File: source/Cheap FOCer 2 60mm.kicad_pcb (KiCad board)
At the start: 2 copper layers, 59.1 x 99.9 mm, 216 parts, among them J1 Conn_01x02, J2 Conn_01x07, J3 Conn_01x03, J4 On/Off, J5 UNUSED MCU PINS, J6 Conn_01x03, P1 MOTOR1, P2 MOTOR1, P3 MOTOR1, P4 HALL/Encoder, P5 SWD, Q1 NCEP60T20, Q2 NCEP60T20, Q3 NCEP60T20, Q4 NCEP60T20, Q5 NCEP60T20, Q6 NCEP60T20, U1 AMS1117-3.3, U2 DRV8301, U3 TP2604-SR, U4 TJA1051T/3/1J, U5 STM32F405RGT6, U6 BMI160, X1 8MHz 10ppm (X50328MSB2GI)

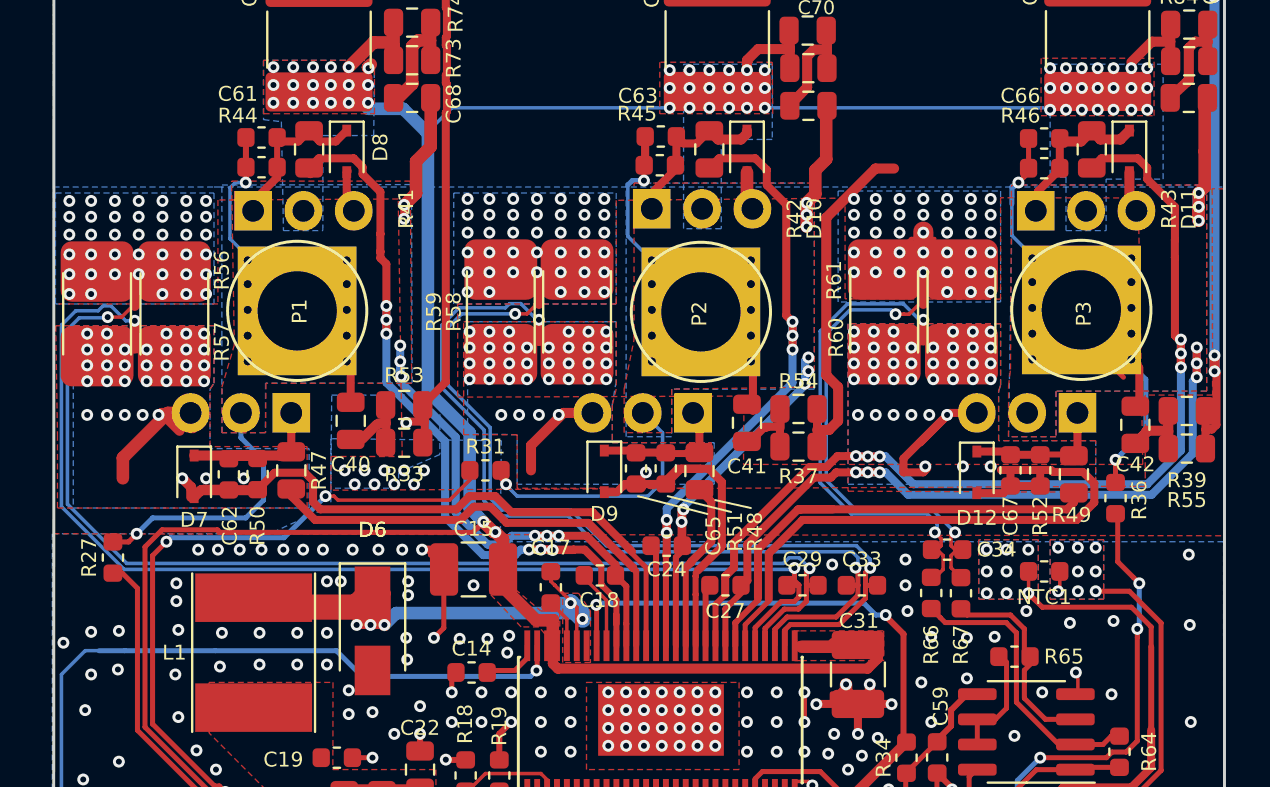
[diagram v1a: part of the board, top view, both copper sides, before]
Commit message: Revert "Remove transistors"
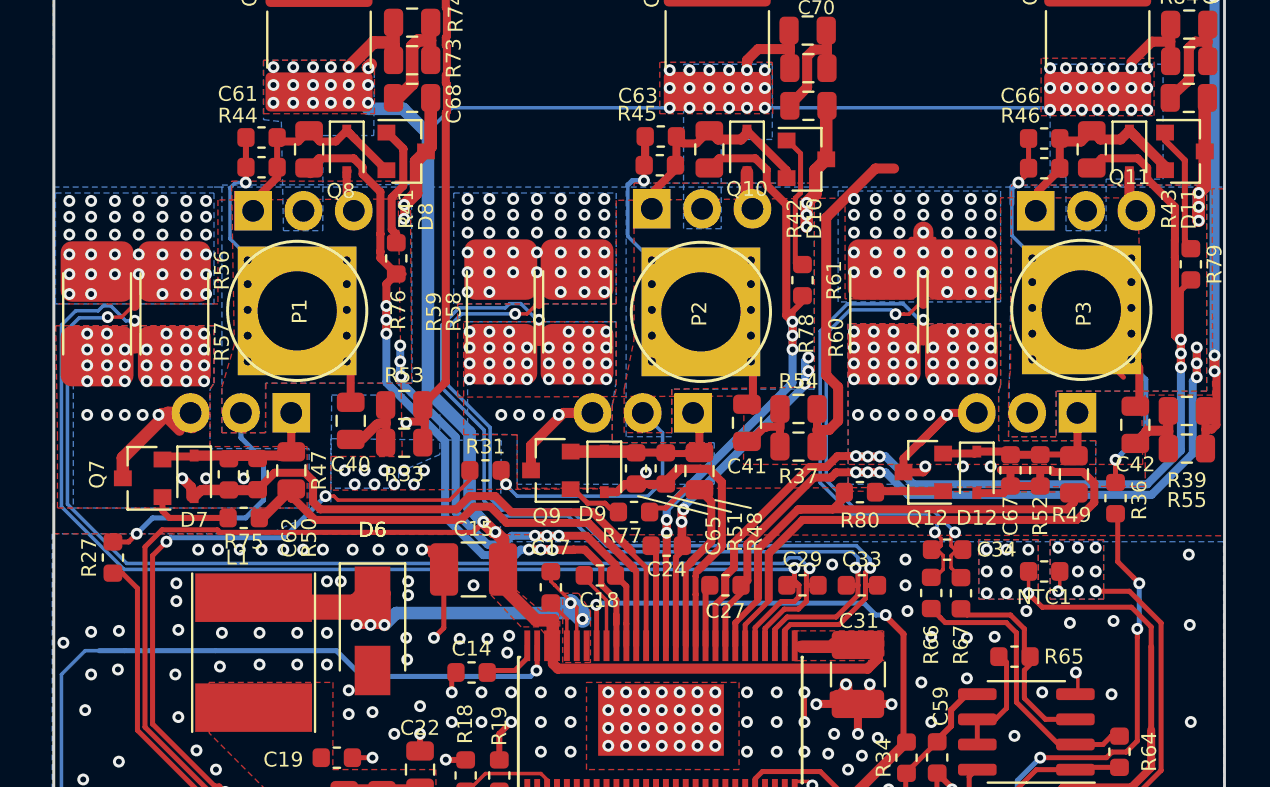
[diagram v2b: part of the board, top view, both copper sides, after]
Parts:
- added Q10: Q_PNP_BCE, Package_TO_SOT_SMD:SOT-23, F.Cu at (148.6, 93.8)
- added Q11: Q_PNP_BCE, Package_TO_SOT_SMD:SOT-23, F.Cu at (167.7, 93.4)
- added Q12: Q_PNP_BCE, Package_TO_SOT_SMD:SOT-23, F.Cu at (154.5, 109.6)
- added Q7: Q_PNP_BCE, Package_TO_SOT_SMD:SOT-23, F.Cu at (115.1, 109.9)
- added Q8: Q_PNP_BCE, Package_TO_SOT_SMD:SOT-23, F.Cu at (128.4, 93.4)
- added Q9: Q_PNP_BCE, Package_TO_SOT_SMD:SOT-23, F.Cu at (135.7, 109.5)
- added R75: 4.7R, Resistor_SMD:R_0603_1608Metric, F.Cu at (120.2, 111.9)
- added R76: 4.7R, Resistor_SMD:R_0603_1608Metric, F.Cu at (127.9, 98.8)
- added R77: 4.7R, Resistor_SMD:R_0603_1608Metric, F.Cu at (139.9, 111.6)
- added R78: 4.7R, Resistor_SMD:R_0603_1608Metric, F.Cu at (148.4, 99.9)
- added R79: 4.7R, Resistor_SMD:R_0603_1608Metric, F.Cu at (168.0, 99.1)
- added R80: 4.7R, Resistor_SMD:R_0603_1608Metric, F.Cu at (151.3, 110.6)
- R41, R42, R43, R47, R48, R49: value 10R -> 4.7R
- R56, R57, R58, R59, R60, R61: value 0.001R -> 0.002R
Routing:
- net Net-(Q10-Pad1): track 0.00 -> 7.33 mm
- net Net-(Q11-Pad1): track 0.00 -> 6.73 mm
- net Net-(Q8-Pad1): track 0.00 -> 6.63 mm
- net Net-(Q7-Pad1): track 0.00 -> 4.16 mm
- net Net-(C61-Pad1): track 10.4 -> 14.1 mm
- net /Mosfet driver/GH_C: track 54.3 -> 58.0 mm
- net Net-(Q12-Pad1): track 0.00 -> 3.60 mm
- net Net-(C66-Pad1): track 9.52 -> 12.8 mm
- net Net-(C65-Pad1): track 9.83 -> 13.1 mm
- net Net-(C63-Pad1): track 10.1 -> 13.3 mm
- net /Mosfet driver/GL_B: track 9.06 -> 12.0 mm
- net Net-(Q9-Pad1): track 0.00 -> 2.81 mm
- net Net-(C62-Pad1): track 12.0 -> 14.6 mm
- net /Mosfet driver/GL_A: track 23.7 -> 26.0 mm
- net Net-(C67-Pad1): track 7.23 -> 8.97 mm
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
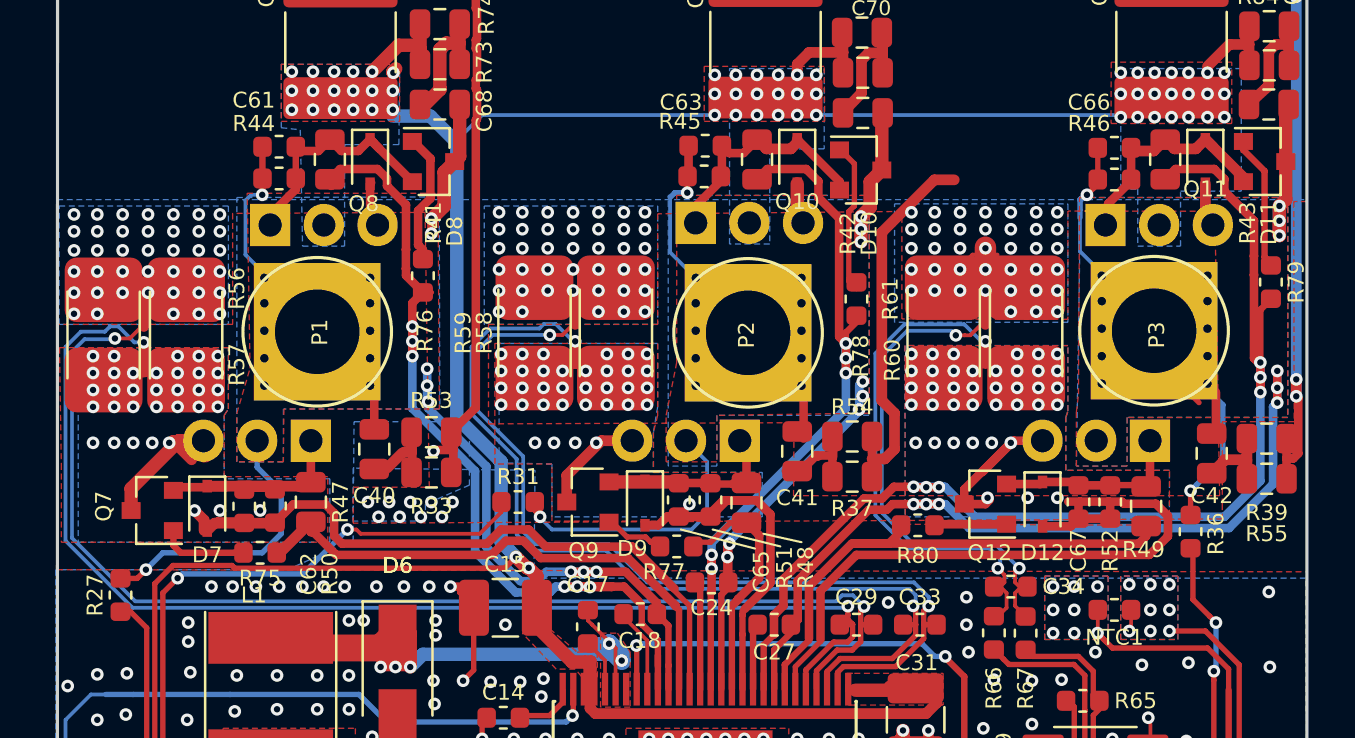
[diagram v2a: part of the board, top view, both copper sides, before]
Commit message: removed transistors from the gate of the mosfets and fixed the config file for compiling the firmware
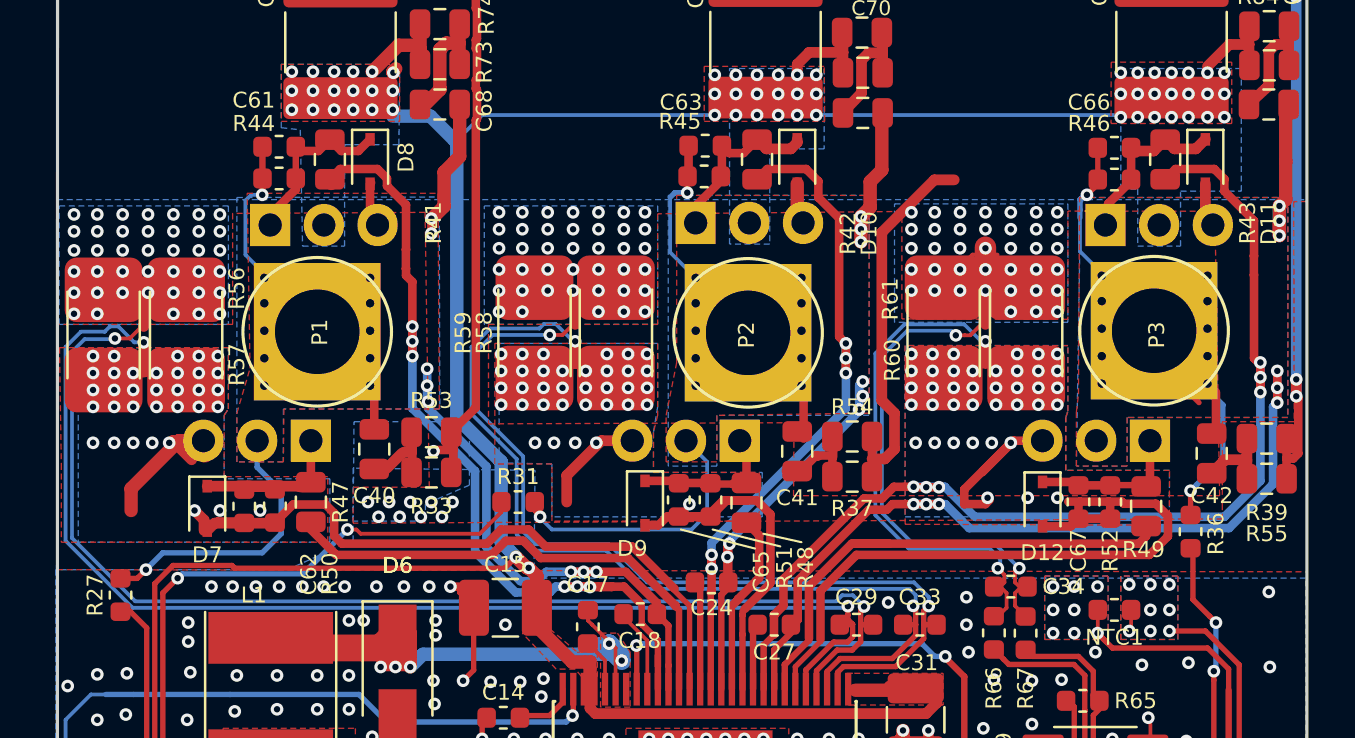
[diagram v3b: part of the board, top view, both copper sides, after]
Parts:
- removed Q10, Q11, Q12, Q7, Q8, Q9: Q_PNP_BCE, Package_TO_SOT_SMD:SOT-23
- removed R75, R76, R77, R78, R79, R80: 4.7R, Resistor_SMD:R_0603_1608Metric
- R41, R42, R43, R47, R48, R49: value 4.7R -> 10R
- R56, R57, R58, R59, R60, R61: value 0.002R -> 0.001R
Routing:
- net Net-(Q10-Pad1): track 7.33 -> 0.00 mm
- net Net-(Q11-Pad1): track 6.73 -> 0.00 mm
- net Net-(Q8-Pad1): track 6.63 -> 0.00 mm
- net Net-(Q7-Pad1): track 4.16 -> 0.00 mm
- net Net-(C61-Pad1): track 14.1 -> 10.4 mm
- net /Mosfet driver/GH_C: track 58.0 -> 54.3 mm
- net Net-(Q12-Pad1): track 3.60 -> 0.00 mm
- net Net-(C66-Pad1): track 12.8 -> 9.52 mm
- net Net-(C65-Pad1): track 13.1 -> 9.83 mm
- net Net-(C63-Pad1): track 13.3 -> 10.1 mm
- net /Mosfet driver/GL_B: track 12.0 -> 9.06 mm
- net Net-(Q9-Pad1): track 2.81 -> 0.00 mm
- net Net-(C62-Pad1): track 14.6 -> 12.0 mm
- net /Mosfet driver/GL_A: track 26.0 -> 23.7 mm
- net Net-(C67-Pad1): track 8.97 -> 7.23 mm
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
